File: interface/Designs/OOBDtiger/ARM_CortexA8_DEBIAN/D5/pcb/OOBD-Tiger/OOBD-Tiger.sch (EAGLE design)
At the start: 122 parts, among them IC1 ADM3053M, IC2 ADM3053M, IC4 DS3231, U1 SY6280, U10 MP1482DS, U2 SN65HVD230(SO8), U3 SY6280, U6 SN65HVD230(SO8)

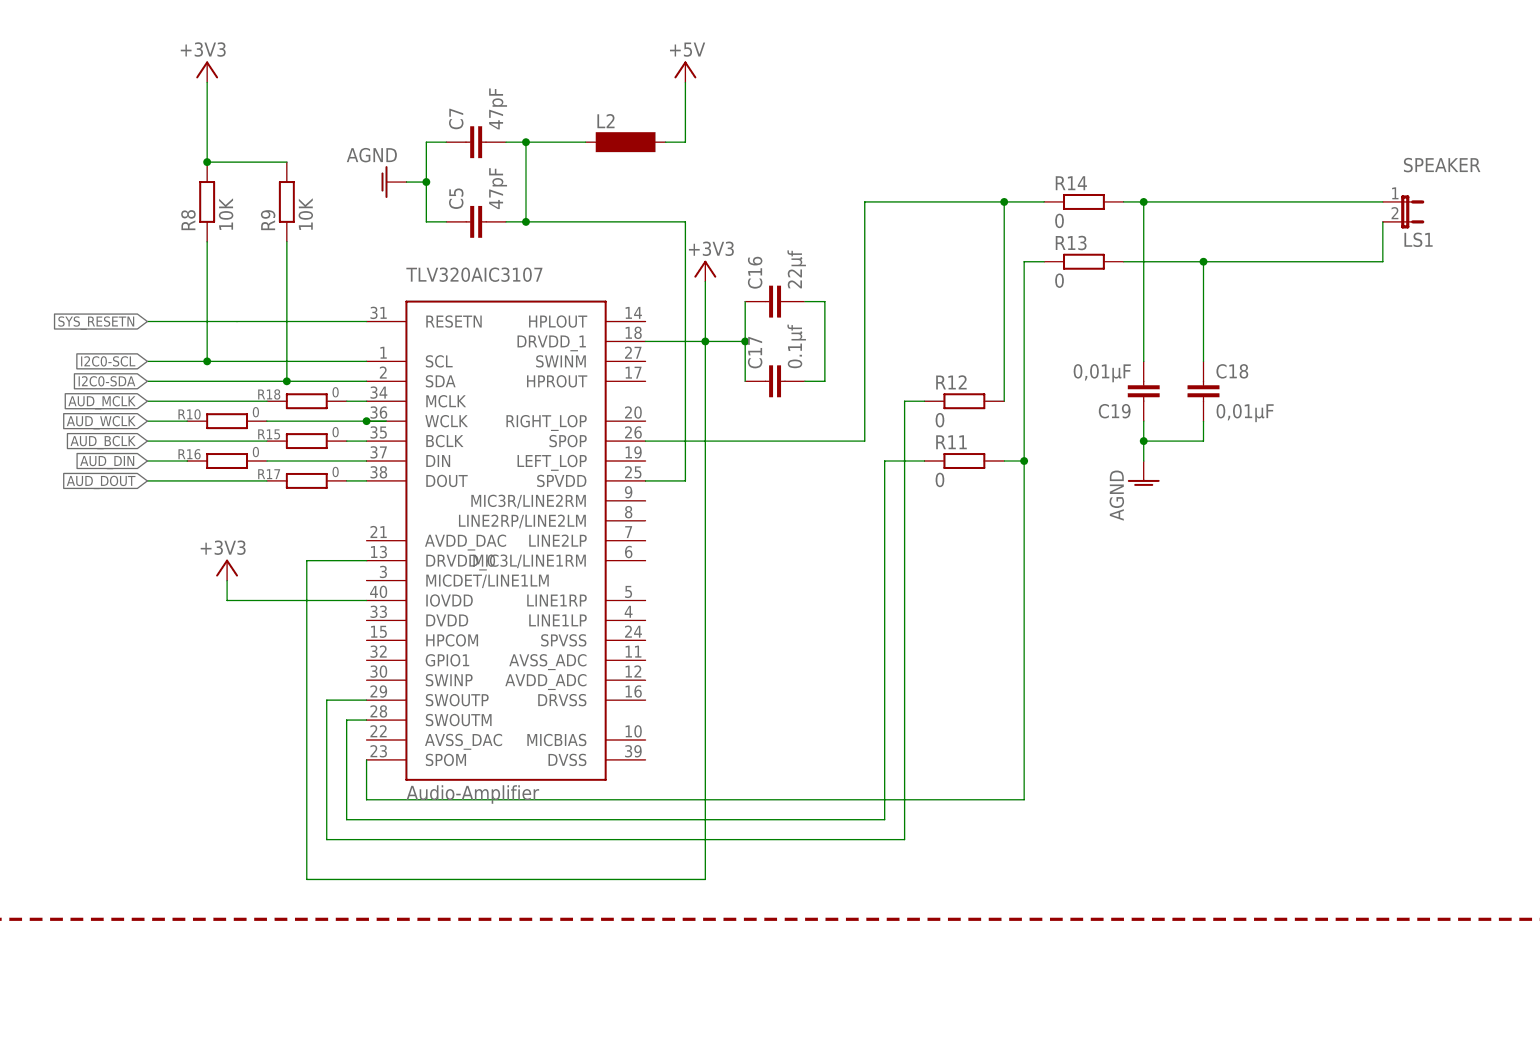
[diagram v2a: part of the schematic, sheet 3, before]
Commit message: further optimization of component placing (now 97,3%) => only audio chip is lacking due to missing power supply connections and missing 1V8 LDO :-(
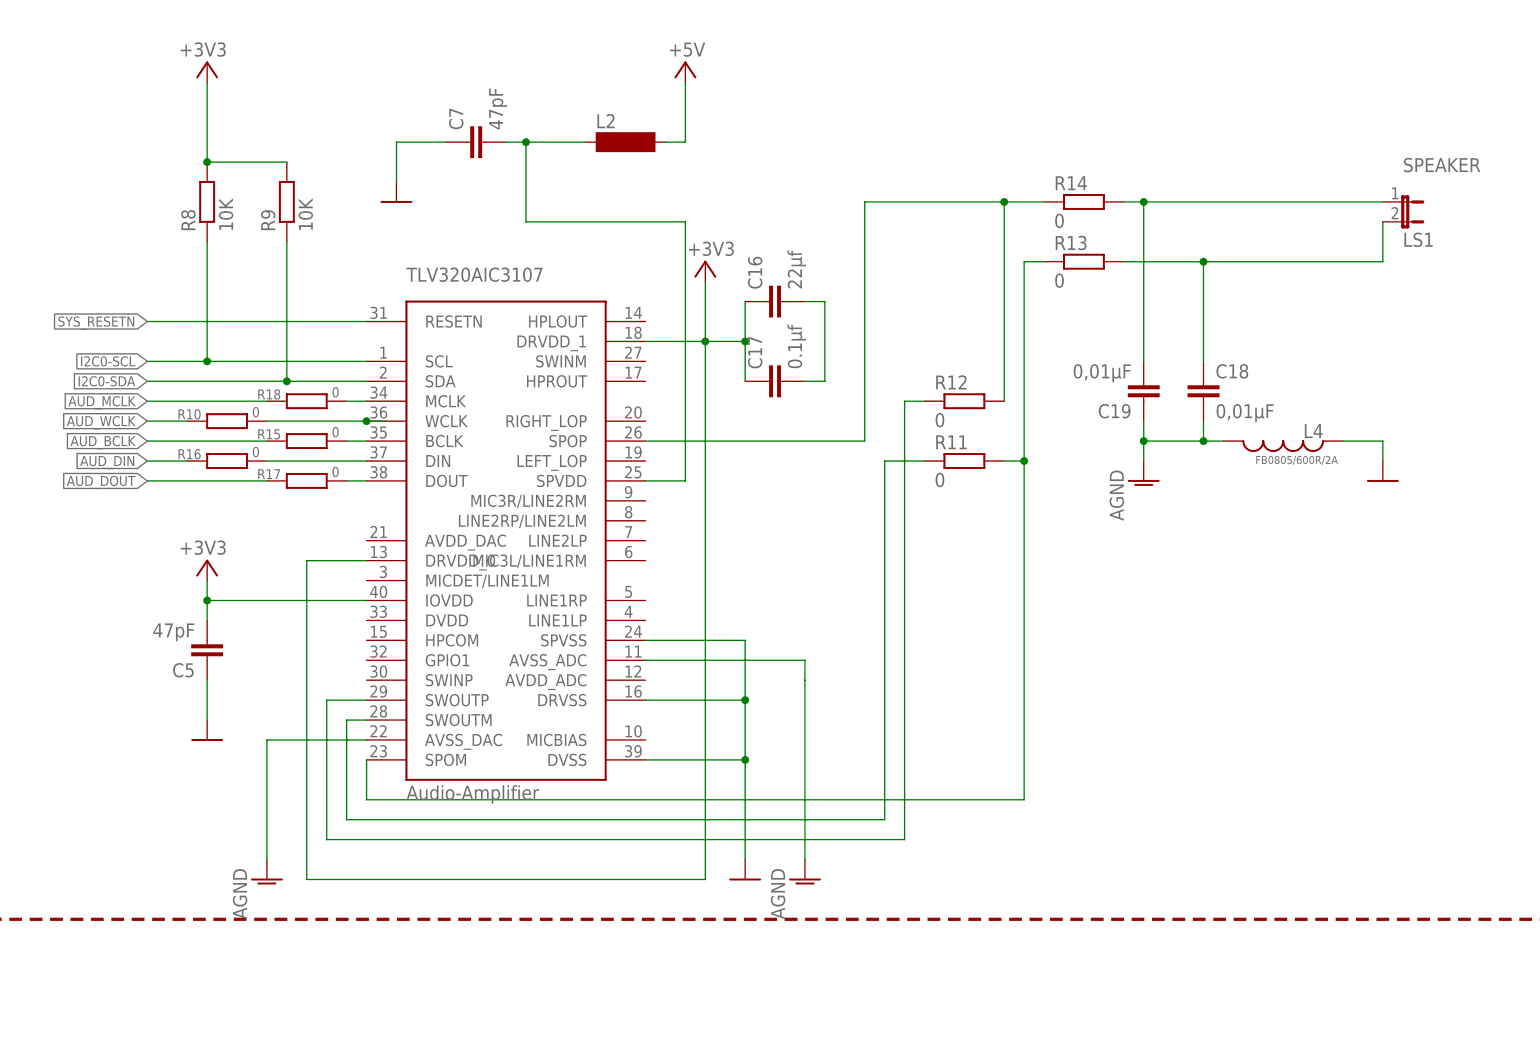
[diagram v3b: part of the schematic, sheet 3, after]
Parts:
- added L4: FB0805/600R/2A, rcl:L-USL0603
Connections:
- net +3V3: now also C5.2
- net AGND: now also L4.2, TLV320AIC3107.AVSS_ADC, TLV320AIC3107.AVSS_DAC; no longer C5.1, C7.1
- net GND: now also C5.1, C7.1, L4.1, TLV320AIC3107.DRVSS, TLV320AIC3107.DVSS, TLV320AIC3107.SPVSS
- net N$17: no longer C5.2
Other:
- moved on the sheet: C5
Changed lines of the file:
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@@
 <setting verticaltext="up"/>
 </settings>
-<grid distance="0.1" unitdist="inch" unit="inch" style="lines" multiple="1" display="no" altdistance="0.01" altunitdist="inch" altunit="inch"/>
+<grid distance="50" unitdist="mil" unit="mil" style="lines" multiple="1" display="yes" altdistance="0.01" altunitdist="inch" altunit="inch"/>
 <layers>
 <layer number="1" name="Top" color="4" fill="1" visible="no" active="no"/>
@@
 <part name="R10" library="resistor" deviceset="R-EU_" device="R0603" value="0"/>
 <part name="R11" library="resistor" deviceset="R-EU_" device="R0603" value="0"/>
-<part name="AGND1" library="supply1" deviceset="AGND" device=""/>
 <part name="C16" library="SparkFun-Passives" deviceset="CAP" device="0603-CAP" value="22µf">
 <attribute name="MANEX" value="123-0001032"/>
@@
 <part name="+3V11" library="supply1" deviceset="+3V3" device=""/>
 <part name="C14" library="rcl" deviceset="C-EU" device="C0805K" value="10µF"/>
+<part name="L4" library="rcl" deviceset="L-US" device="L0603" value="FB0805/600R/2A"/>
+<part name="GND58" library="supply1" deviceset="GND" device="" value=""/>
+<part name="GND59" library="supply1" deviceset="GND" device="" value=""/>
+<part name="GND62" library="supply1" deviceset="GND" device="" value=""/>
+<part name="AGND3" library="supply1" deviceset="AGND" device=""/>
+<part name="AGND4" library="supply1" deviceset="AGND" device=""/>
+<part name="GND63" library="supply1" deviceset="GND" device="" value=""/>
 </parts>
 <sheets>
@@
 <attribute name="MANEX" x="53.34" y="210.82" size="1.778" layer="96" rot="R90" display="off"/>
 </instance>
-<instance part="C5" gate="G$1" x="78.74" y="208.28" rot="R90">
-<attribute name="MANEX" x="78.74" y="208.28" size="1.778" layer="96" rot="R90" display="off"/>
+<instance part="C5" gate="G$1" x="43.18" y="154.94" rot="R180">
+<attribute name="MANEX" x="43.18" y="154.94" size="1.778" layer="96" rot="R180" display="off"/>
 </instance>
 <instance part="C7" gate="G$1" x="78.74" y="218.44" rot="R90">
@@
 </instance>
 <instance part="R11" gate="G$1" x="139.7" y="177.8"/>
-<instance part="AGND1" gate="VR1" x="66.04" y="213.36" rot="R270"/>
 <instance part="C16" gate="G$1" x="116.84" y="198.12" rot="R90">
 <attribute name="MANEX" x="116.84" y="198.12" size="1.778" layer="96" rot="R90" display="off"/>
@@
 <attribute name="VALUE" x="106.68" y="231.14" size="1.778" layer="96" rot="R180"/>
 </instance>
-<instance part="+3V5" gate="G$1" x="45.72" y="165.1" smashed="yes">
-<attribute name="VALUE" x="48.26" y="167.64" size="1.778" layer="96" rot="R180"/>
+<instance part="+3V5" gate="G$1" x="43.18" y="165.1" smashed="yes">
+<attribute name="VALUE" x="45.72" y="167.64" size="1.778" layer="96" rot="R180"/>
 </instance>
 <instance part="+3V6" gate="G$1" x="106.68" y="203.2" smashed="yes">
 <attribute name="VALUE" x="110.49" y="205.74" size="1.778" layer="96" rot="R180"/>
 </instance>
+<instance part="L4" gate="G$1" x="180.34" y="180.34" smashed="yes" rot="R270">
+<attribute name="NAME" x="182.88" y="182.499" size="1.778" layer="95" rot="MR180"/>
+<attribute name="VALUE" x="187.325" y="178.435" size="1.016" layer="96" rot="R180"/>
+</instance>
+<instance part="GND58" gate="1" x="193.04" y="175.26"/>
+<instance part="GND59" gate="1" x="43.18" y="142.24"/>
+<instance part="GND62" gate="1" x="111.76" y="124.46"/>
+<instance part="AGND3" gate="VR1" x="119.38" y="124.46"/>
+<instance part="AGND4" gate="VR1" x="50.8" y="124.46"/>
+<instance part="GND63" gate="1" x="67.31" y="210.82"/>
 </instances>
 <busses>
@@
 </net>
 <net name="AGND" class="0">
-<segment>
-<pinref part="AGND1" gate="VR1" pin="AGND"/>
-<pinref part="C7" gate="G$1" pin="1"/>
-<wire x1="68.58" y1="213.36" x2="71.12" y2="213.36" width="0.1524" layer="91"/>
-<wire x1="73.66" y1="208.28" x2="71.12" y2="208.28" width="0.1524" layer="91"/>
-<wire x1="71.12" y1="208.28" x2="71.12" y2="213.36" width="0.1524" layer="91"/>
-<wire x1="71.12" y1="213.36" x2="71.12" y2="218.44" width="0.1524" layer="91"/>
-<wire x1="71.12" y1="218.44" x2="73.66" y2="218.44" width="0.1524" layer="91"/>
-<pinref part="C5" gate="G$1" pin="1"/>
-<junction x="71.12" y="213.36"/>
-</segment>
 <segment>
 <pinref part="AGND2" gate="VR1" pin="AGND"/>
@@
 <wire x1="170.18" y1="180.34" x2="170.18" y2="182.88" width="0.1524" layer="91"/>
 <junction x="162.56" y="180.34"/>
+<pinref part="L4" gate="G$1" pin="2"/>
+<wire x1="170.18" y1="180.34" x2="172.72" y2="180.34" width="0.1524" layer="91"/>
+<junction x="170.18" y="180.34"/>
+</segment>
+<segment>
+<pinref part="AGND3" gate="VR1" pin="AGND"/>
+<pinref part="TLV320AIC3107" gate="G$1" pin="AVSS_ADC"/>
+<wire x1="119.38" y1="127" x2="119.38" y2="149.86" width="0.1524" layer="91"/>
+<wire x1="119.38" y1="149.86" x2="119.38" y2="152.4" width="0.1524" layer="91"/>
+<wire x1="119.38" y1="152.4" x2="99.06" y2="152.4" width="0.1524" layer="91"/>
+</segment>
+<segment>
+<pinref part="TLV320AIC3107" gate="G$1" pin="AVSS_DAC"/>
+<pinref part="AGND4" gate="VR1" pin="AGND"/>
+<wire x1="63.5" y1="142.24" x2="50.8" y2="142.24" width="0.1524" layer="91"/>
+<wire x1="50.8" y1="142.24" x2="50.8" y2="127" width="0.1524" layer="91"/>
 </segment>
 </net>
@@
 <wire x1="99.06" y1="175.26" x2="104.14" y2="175.26" width="0.1524" layer="91"/>
 <wire x1="104.14" y1="175.26" x2="104.14" y2="208.28" width="0.1524" layer="91"/>
-<pinref part="C5" gate="G$1" pin="2"/>
 <wire x1="104.14" y1="208.28" x2="83.82" y2="208.28" width="0.1524" layer="91"/>
-<wire x1="81.28" y1="208.28" x2="83.82" y2="208.28" width="0.1524" layer="91"/>
 <wire x1="83.82" y1="208.28" x2="83.82" y2="218.44" width="0.1524" layer="91"/>
 <pinref part="C7" gate="G$1" pin="2"/>
 <wire x1="83.82" y1="218.44" x2="81.28" y2="218.44" width="0.1524" layer="91"/>
-<junction x="83.82" y="208.28"/>
 <junction x="83.82" y="218.44"/>
 <pinref part="L2" gate="G$1" pin="1"/>
@@
 <segment>
 <pinref part="TLV320AIC3107" gate="G$1" pin="IOVDD"/>
-<wire x1="63.5" y1="160.02" x2="45.72" y2="160.02" width="0.1524" layer="91"/>
-<wire x1="45.72" y1="160.02" x2="45.72" y2="162.56" width="0.1524" layer="91"/>
+<wire x1="63.5" y1="160.02" x2="43.18" y2="160.02" width="0.1524" layer="91"/>
+<wire x1="43.18" y1="160.02" x2="43.18" y2="162.56" width="0.1524" layer="91"/>
 <pinref part="+3V5" gate="G$1" pin="+3V3"/>
+<pinref part="C5" gate="G$1" pin="2"/>
+<wire x1="43.18" y1="160.02" x2="43.18" y2="157.48" width="0.1524" layer="91"/>
+<junction x="43.18" y="160.02"/>
 </segment>
 <segment>
@@
 </segment>
 </net>
+<net name="GND" class="1">
+<segment>
+<pinref part="L4" gate="G$1" pin="1"/>
+<pinref part="GND58" gate="1" pin="GND"/>
+<wire x1="187.96" y1="180.34" x2="193.04" y2="180.34" width="0.1524" layer="91"/>
+<wire x1="193.04" y1="180.34" x2="193.04" y2="177.8" width="0.1524" layer="91"/>
+</segment>
+<segment>
+<pinref part="C5" gate="G$1" pin="1"/>
+<pinref part="GND59" gate="1" pin="GND"/>
+<wire x1="43.18" y1="149.86" x2="43.18" y2="144.78" width="0.1524" layer="91"/>
+</segment>
+<segment>
+<pinref part="TLV320AIC3107" gate="G$1" pin="DRVSS"/>
+<pinref part="GND62" gate="1" pin="GND"/>
+<wire x1="99.06" y1="147.32" x2="111.76" y2="147.32" width="0.1524" layer="91"/>
+<wire x1="111.76" y1="147.32" x2="111.76" y2="139.7" width="0.1524" layer="91"/>
+<pinref part="TLV320AIC3107" gate="G$1" pin="DVSS"/>
+<wire x1="111.76" y1="139.7" x2="111.76" y2="127" width="0.1524" layer="91"/>
+<wire x1="99.06" y1="139.7" x2="111.76" y2="139.7" width="0.1524" layer="91"/>
+<junction x="111.76" y="139.7"/>
+<pinref part="TLV320AIC3107" gate="G$1" pin="SPVSS"/>
+<wire x1="99.06" y1="154.94" x2="111.76" y2="154.94" width="0.1524" layer="91"/>
+<wire x1="111.76" y1="154.94" x2="111.76" y2="147.32" width="0.1524" layer="91"/>
+<junction x="111.76" y="147.32"/>
+</segment>
+<segment>
+<pinref part="C7" gate="G$1" pin="1"/>
+<wire x1="67.31" y1="218.44" x2="73.66" y2="218.44" width="0.1524" layer="91"/>
+<pinref part="GND63" gate="1" pin="GND"/>
+<wire x1="67.31" y1="213.36" x2="67.31" y2="218.44" width="0.1524" layer="91"/>
+</segment>
+</net>

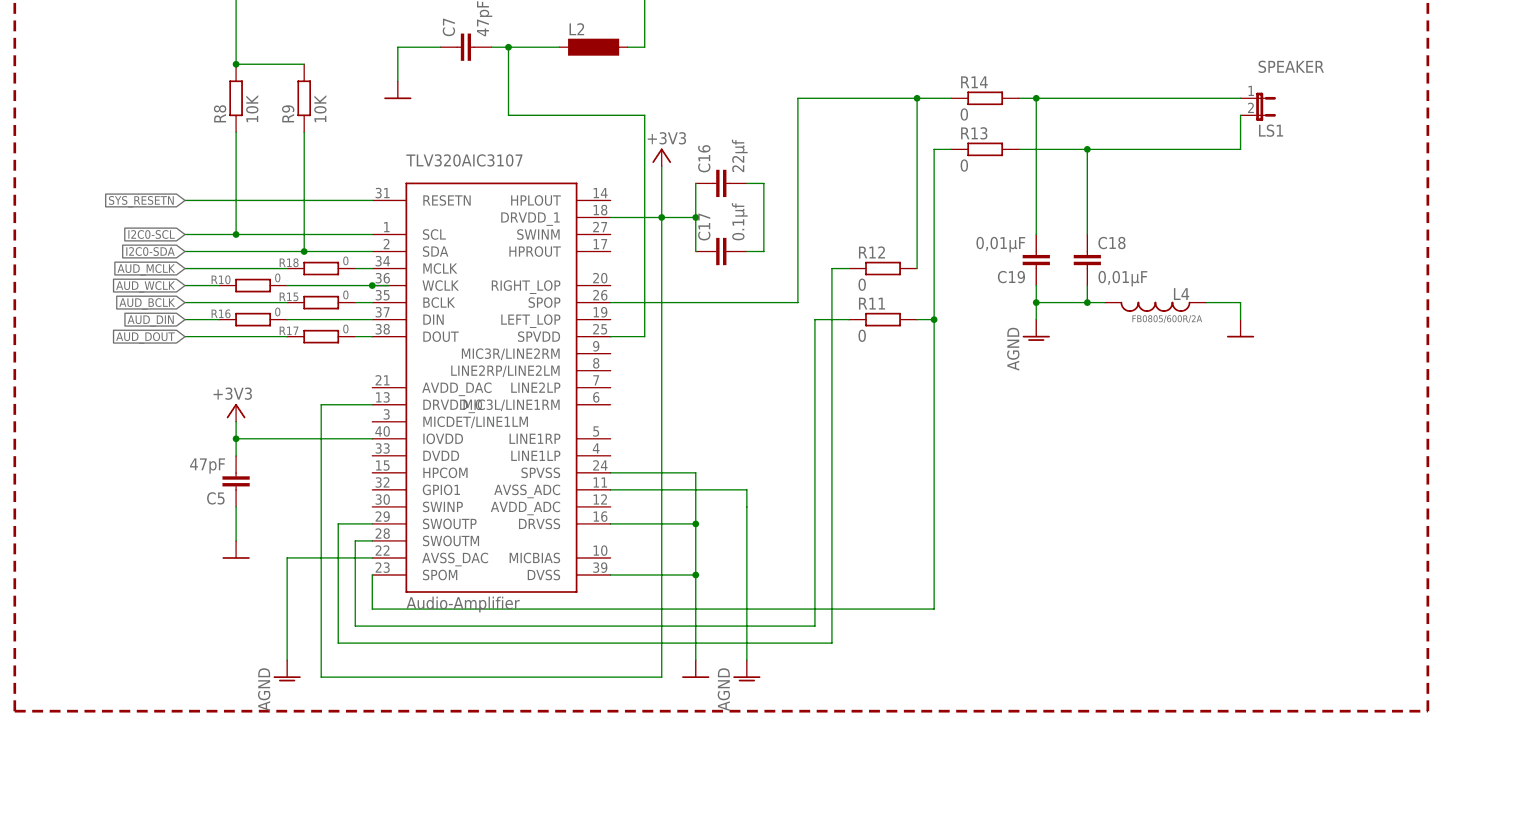
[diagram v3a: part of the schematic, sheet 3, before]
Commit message: add missing 1V8 LDO (97,1% autorouting now)
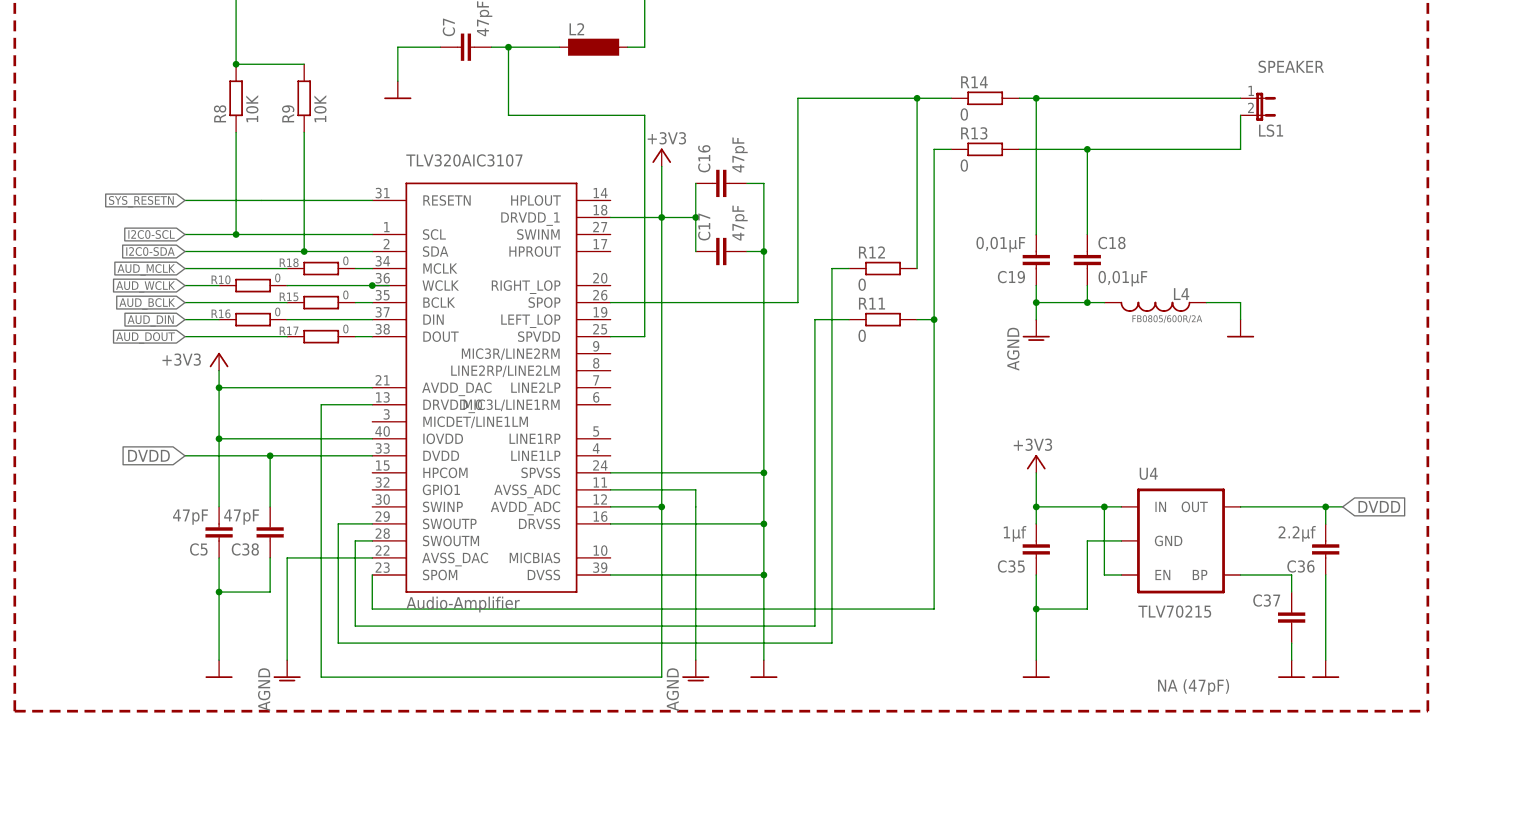
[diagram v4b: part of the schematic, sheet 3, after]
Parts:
- added C35: 1µf, SparkFun-Passives:CAP0603-CAP
- added C36: 2.2µf, SparkFun-Passives:CAP0603-CAP
- added C37: NA (47pF), SparkFun-Passives:CAP0603-CAP
- added C38: 47pF, SparkFun-Passives:CAP0603-CAP
- added U4: TLV70215, SparkFun-PowerIC:V_REG_LDOSMD
- C16: value 22µf -> 47pF
- C17: value 0.1µf -> 47pF
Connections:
- removed net N$16: C16.2, C17.2
- new net DVDD: C36.2, C38.2, TLV320AIC3107.DVDD, U4.OUT
- new net N$12: C37.2, U4.BP
- net +3V3: now also C35.2, TLV320AIC3107.AVDD_ADC, TLV320AIC3107.AVDD_DAC, U4.EN, U4.IN
- net GND: now also C16.2, C17.2, C35.1, C36.1, C37.1, C38.1, U4.GND
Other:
- moved on the sheet: C5
